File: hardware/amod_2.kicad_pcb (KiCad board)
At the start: 4 copper layers, 100 x 100 mm, 101 parts, among them J101 USB-C, J201 SMA, J202 SMA, J301 SMA, J302 SMA, J303 SMA, J304 SMA, J501 SMA, J502 SMA, J503 SMA, J504 SMA, J505 Pmod, Q301 AO3401A, Q501 AO3401A, SW301 ON, SW501 ON, U101 TPS65131, U102 LM2664, U201 THS3491, U301 OPA847, U501 LMH6629, U502 LMH6629

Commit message: AMOD-2 in progress: Y9 switched noise source, Y7 reflection bridge (INC and REFL = 2A - 2B), Y8 passive coupled resonators with capacitive ports
ERC 0, DRC 0.  IO8 reaches Y9 round the left and top margins; Y9's -5 V up a finger of L3 from the gutter.

Co-Authored-By: Claude Opus 5.5 <noreply@anthropic.com>
Claude-Session: https://claude.ai/code/session_01RKeoKvFFzjk3cEBLCXXHnB
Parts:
- added C701: 100n, Capacitor_SMD:C_0402_1005Metric, F.Cu at (23.4, 31.2)
- added C702: 100n, Capacitor_SMD:C_0402_1005Metric, F.Cu at (28.6, 31.2)
- added C703: 100n, Capacitor_SMD:C_0402_1005Metric, F.Cu at (16.9, 40.9)
- added C704: 100n, Capacitor_SMD:C_0402_1005Metric, F.Cu at (30.6, 42.8)
- added C801: 2.2p, Capacitor_SMD:C_0402_1005Metric, F.Cu at (18.1, 55.5)
- added C802: 4.7p, Capacitor_SMD:C_0402_1005Metric, F.Cu at (18.6, 53.5)
- added C803: 2.2p, Capacitor_SMD:C_0402_1005Metric, F.Cu at (23.0, 61.4)
- added C804: 1p, Capacitor_SMD:C_0402_1005Metric, F.Cu at (25.4, 57.1)
- added C805: 2.2p, Capacitor_SMD:C_0402_1005Metric, F.Cu at (26.6, 57.1)
- added C806: 1n, Capacitor_SMD:C_0402_1005Metric, F.Cu at (38.5, 53.4)
- added C807: 6.8p, Capacitor_SMD:C_0402_1005Metric, F.Cu at (45.8, 57.4)
- added C808: 2.2p, Capacitor_SMD:C_0402_1005Metric, F.Cu at (44.5, 61.4)
- added C809: 100n, Capacitor_SMD:C_0402_1005Metric, F.Cu at (16.8, 63.0)
- added C901: 1u, Capacitor_SMD:C_0402_1005Metric, F.Cu at (75.5, 8.35)
- added C902: 100n, Capacitor_SMD:C_0402_1005Metric, F.Cu at (78.6, 11.1)
- added C903: 100p, Capacitor_SMD:C_0402_1005Metric, F.Cu at (79.8, 18.1)
- added C904: 100n, Capacitor_SMD:C_0402_1005Metric, F.Cu at (78.7, 18.1)
- added C905: 1u, Capacitor_SMD:C_0402_1005Metric, F.Cu at (82.7, 12.5)
- added C906: 1u, Capacitor_SMD:C_0402_1005Metric, F.Cu at (83.3, 20.6)
- added C907: 1u, Capacitor_SMD:C_0402_1005Metric, F.Cu at (88.8, 13.3)
- added C908: 100n, Capacitor_SMD:C_0402_1005Metric, F.Cu at (81.2, 20.1)
- added D801: BB133, Diode_SMD:D_SOD-323, F.Cu at (24.9, 53.5)
- added D802: BB133, Diode_SMD:D_SOD-323, F.Cu at (26.9, 53.5)
- added D803: BB133, Diode_SMD:D_SOD-323, F.Cu at (42.6, 53.5)
- added D804: BB133, Diode_SMD:D_SOD-323, F.Cu at (44.8, 53.5)
- added J701: SMA, amod:SMA_BWSMA-KE-Z001_Vertical, F.Cu at (12.5, 34.0)
- added J702: SMA, amod:SMA_BWSMA-KE-Z001_Vertical, F.Cu at (23.0, 44.5)
- added J703: SMA, amod:SMA_BWSMA-KE-Z001_Vertical, F.Cu at (34.0, 34.0)
- added J704: SMA, amod:SMA_BWSMA-KE-Z001_Vertical, F.Cu at (44.5, 44.5)
- added J801: SMA, amod:SMA_BWSMA-KE-Z001_Vertical, F.Cu at (12.5, 55.5)
- added J802: SMA, amod:SMA_BWSMA-KE-Z001_Vertical, F.Cu at (23.0, 66.0)
- added J803: SMA, amod:SMA_BWSMA-KE-Z001_Vertical, F.Cu at (34.0, 55.5)
- added J804: SMA, amod:SMA_BWSMA-KE-Z001_Vertical, F.Cu at (44.5, 66.0)
- added J901: SMA, amod:SMA_BWSMA-KE-Z001_Vertical, F.Cu at (87.5, 23.0)
- added L801: 10u, Inductor_SMD:L_1210_3225Metric, F.Cu at (21.6, 52.6)
- added L802: 10u, Inductor_SMD:L_1210_3225Metric, F.Cu at (47.5, 53.4)
- added Q701: AO3401A, Package_TO_SOT_SMD:SOT-23, F.Cu at (15.3, 47.4)
- added Q801: AO3401A, Package_TO_SOT_SMD:SOT-23, F.Cu at (15.3, 68.8)
- added Q901: AO3401A, Package_TO_SOT_SMD:SOT-23, F.Cu at (79.8, 25.9)
- added Q902: MMBT3904, Package_TO_SOT_SMD:SOT-23, F.Cu at (78.8, 15.3)
- added R701: 49.9, Resistor_SMD:R_0402_1005Metric, F.Cu at (20.9, 34.0)
- added R702: 49.9, Resistor_SMD:R_0402_1005Metric, F.Cu at (19.9, 35.5)
- added R703: 49.9, Resistor_SMD:R_0402_1005Metric, F.Cu at (19.9, 37.5)
- added R704: 499, Resistor_SMD:R_0402_1005Metric, F.Cu at (22.6, 40.4)
- added R705: 499, Resistor_SMD:R_0402_1005Metric, F.Cu at (20.6, 40.4)
- added R706: 49.9, Resistor_SMD:R_0402_1005Metric, F.Cu at (24.6, 39.9)
- added R707: 499, Resistor_SMD:R_0402_1005Metric, F.Cu at (25.2, 37.6)
- added R708: 499, Resistor_SMD:R_0402_1005Metric, F.Cu at (27.6, 40.4)
- added R709: 49.9, Resistor_SMD:R_0402_1005Metric, F.Cu at (31.2, 39.2)
- added R801: 49.9, Resistor_SMD:R_0402_1005Metric, F.Cu at (16.6, 56.9)
- added R802: 100k, Resistor_SMD:R_0402_1005Metric, F.Cu at (28.8, 53.1)
- added R803: 100k, Resistor_SMD:R_0402_1005Metric, F.Cu at (28.8, 55.1)
- added R804: 2k, Resistor_SMD:R_0402_1005Metric, F.Cu at (27.8, 57.1)
- added R805: 100k, Resistor_SMD:R_0402_1005Metric, F.Cu at (39.6, 53.4)
- added R806: 100k, Resistor_SMD:R_0402_1005Metric, F.Cu at (40.9, 53.4)
- added R807: 2k, Resistor_SMD:R_0402_1005Metric, F.Cu at (39.0, 57.4)
- added R901: 680, Resistor_SMD:R_0402_1005Metric, F.Cu at (78.6, 12.7)
- added R902: 10k, Resistor_SMD:R_0402_1005Metric, F.Cu at (83.8, 11.1)
- added R903: 10k, Resistor_SMD:R_0402_1005Metric, F.Cu at (84.9, 11.1)
- added R904: 240, Resistor_SMD:R_0402_1005Metric, F.Cu at (85.8, 17.9)
- added R905: 27, Resistor_SMD:R_0402_1005Metric, F.Cu at (83.3, 18.6)
- added R906: 49.9, Resistor_SMD:R_0402_1005Metric, F.Cu at (88.8, 15.3)
- added SW701: ON, amod:SW_SPDT_Shouhan_MSK12C02, F.Cu at (10.5, 44.9)
- added SW801: ON, amod:SW_SPDT_Shouhan_MSK12C02, F.Cu at (10.5, 66.3)
- added SW802: DIP4, amod:SW_DIP_SPSTx04_Slide_1.27mm_DSHP04, F.Cu at (33.8, 65.0)
- added SW901: ON, amod:SW_SPDT_Shouhan_MSK12C02, F.Cu at (75.0, 23.4)
- added U701: OPA810, Package_TO_SOT_SMD:SOT-23-5, F.Cu at (22.4, 37.6)
- added U702: OPA810, Package_TO_SOT_SMD:SOT-23-5, F.Cu at (27.6, 37.6)
- added U901: TPS22917, Package_TO_SOT_SMD:SOT-23-6, F.Cu at (75.5, 10.8)
- added U902: LMH6629, Package_TO_SOT_SMD:SOT-23-5, F.Cu at (85.5, 14.7)
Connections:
- J505 pad 5: unconnected-(J505-Pin_5-Pad5) -> /PMOD8
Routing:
- net /PMOD8: track 0.00 -> 188.2 mm
- net /Y8_VS: track 0.00 -> 72.2 mm, vias 0 -> 4
- net /Y8_T2: track 0.00 -> 42.5 mm
- net /Y9_VS: track 0.00 -> 41.0 mm, vias 0 -> 4
- net GND: track 70.1 -> 105.8 mm, vias 57 -> 88
- net /Y7_VS: track 0.00 -> 27.7 mm, vias 0 -> 5
- net -5V: track 62.5 -> 87.7 mm, vias 6 -> 13
- net /Y8_T1: track 0.00 -> 23.3 mm
- net /Y7_REFL: track 0.00 -> 18.0 mm
- net /Y7_A: track 0.00 -> 15.2 mm
- net /Y9_OA: track 0.00 -> 11.0 mm
- net /Y8_RDA: track 0.00 -> 10.2 mm
- net /Y8_CB: track 0.00 -> 10.2 mm
- net /Y8_K2: track 0.00 -> 10.1 mm
- net /Y8_CA: track 0.00 -> 10.1 mm
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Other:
- board text added: "BRIDGE"
- board text added: "DRIVE"
- board text added: "DUT"
- board text added: "INC"
- board text added: "NOISE"
- board text added: "OUT 1"
- board text added: "OUT 2"
- board text added: "REFL"
- board text added: "REFL/INC=S11"
- board text added: "SIG"
- board text added: "TANKS"
- board text added: "TUNE/PUMP"
- board text added: "Y7"
- board text added: "Y8"
- board text added: "Y9"

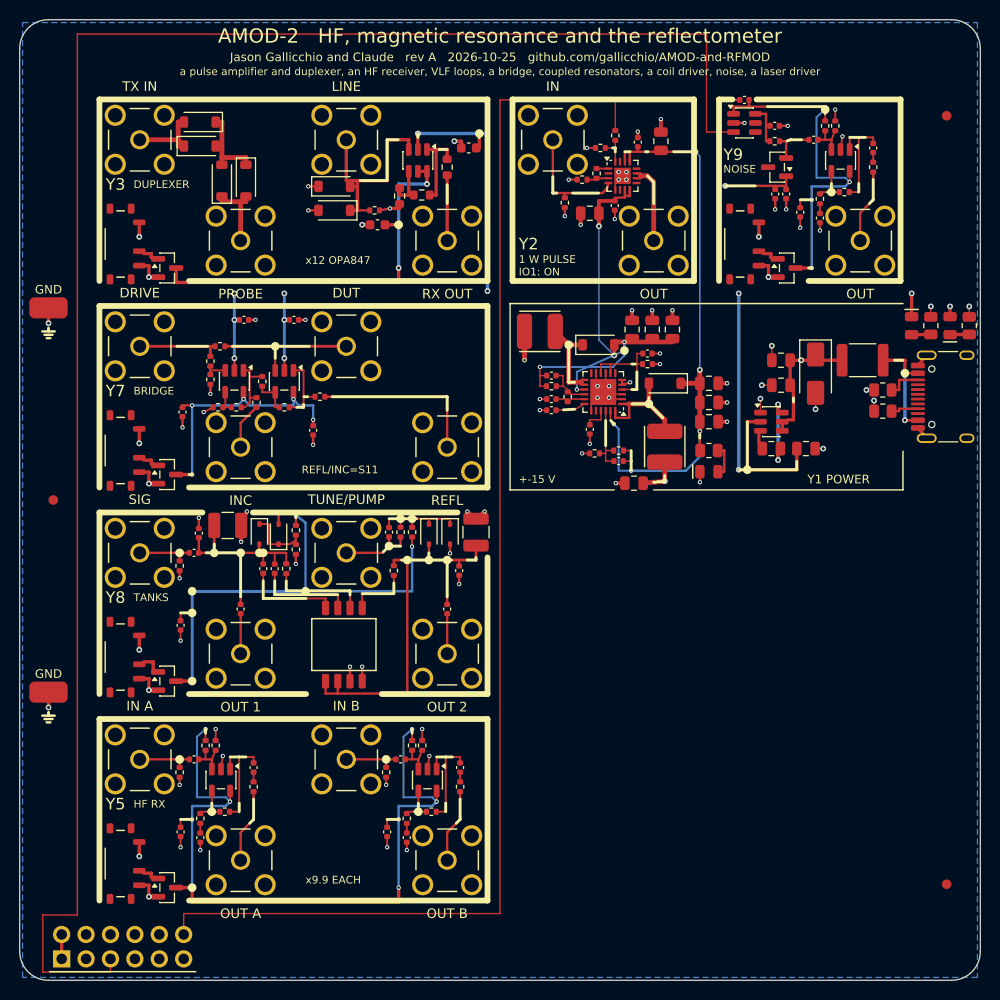
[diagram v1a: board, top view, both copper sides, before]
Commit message: AMOD-2 in progress: Y10 laser driver (100 mA/V high-side source, IO5 shunt, 20 MHz - 3 GHz bias-T, diode-voltage monitor)
ERC 0, DRC 0.  IO5 up the gutter at x 50.4; a foot moved off the LD jack.

Co-Authored-By: Claude Opus 5.5 <noreply@anthropic.com>
Claude-Session: https://claude.ai/code/session_01RKeoKvFFzjk3cEBLCXXHnB
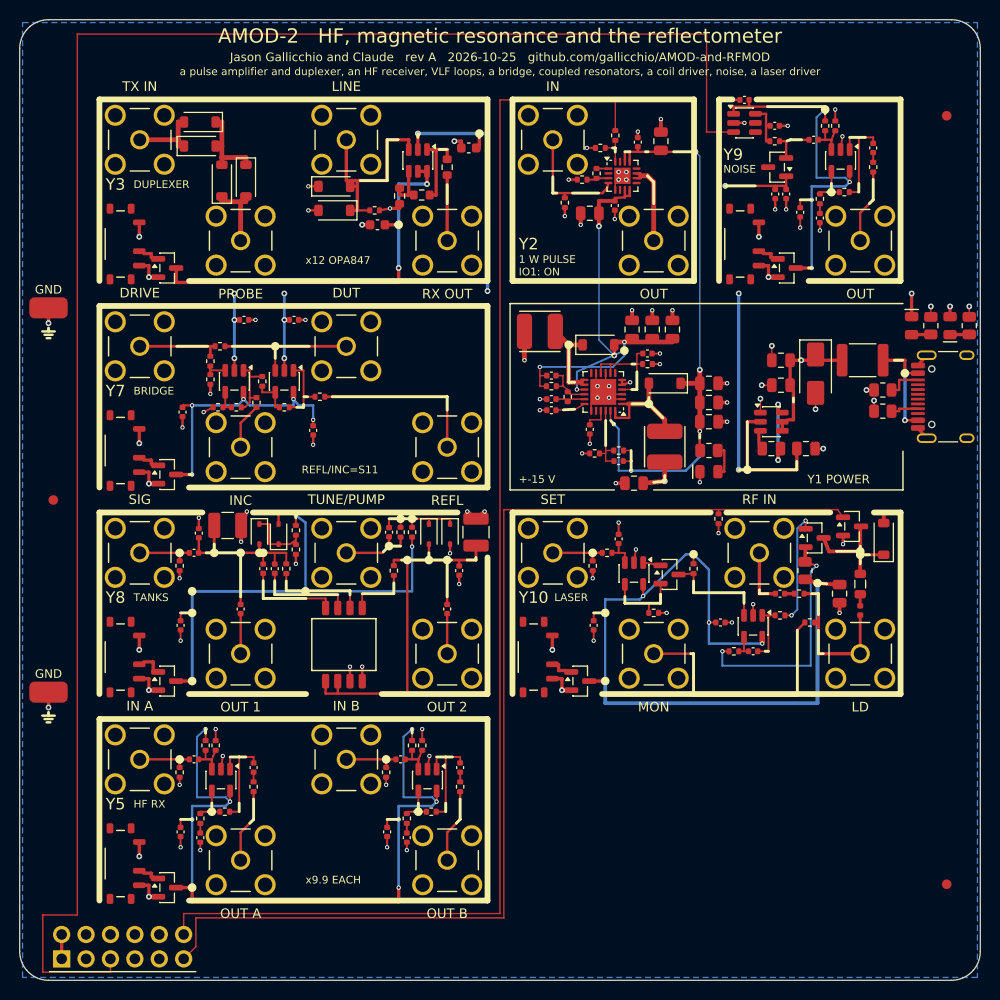
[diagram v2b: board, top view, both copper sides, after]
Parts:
- added C1001: 100n, Capacitor_SMD:C_0402_1005Metric, F.Cu at (62.4, 54.0)
- added C1002: 100n, Capacitor_SMD:C_0402_1005Metric, F.Cu at (59.8, 63.0)
- added C1003: 10n, Capacitor_SMD:C_0402_1005Metric, F.Cu at (76.3, 65.8)
- added C1004: 10u, Capacitor_SMD:C_0805_2012Metric, F.Cu at (85.3, 59.8)
- added C1005: 100p, Capacitor_SMD:C_0402_1005Metric, F.Cu at (79.2, 59.8)
- added C1006: 100n, Capacitor_SMD:C_0402_1005Metric, F.Cu at (73.0, 62.8)
- added D1001: B5819W, Diode_SMD:D_SOD-123, F.Cu at (90.0, 54.0)
- added J1001: SMA, amod:SMA_BWSMA-KE-Z001_Vertical, F.Cu at (55.5, 55.5)
- added J1002: SMA, amod:SMA_BWSMA-KE-Z001_Vertical, F.Cu at (66.0, 66.0)
- added J1003: SMA, amod:SMA_BWSMA-KE-Z001_Vertical, F.Cu at (77.0, 55.5)
- added J1004: SMA, amod:SMA_BWSMA-KE-Z001_Vertical, F.Cu at (87.5, 66.0)
- added L1001: 330n, Inductor_SMD:L_0805_2012Metric, F.Cu at (87.5, 58.8)
- added L1002: 27n, Inductor_SMD:L_0402_1005Metric, F.Cu at (87.5, 61.5)
- added Q1001: AO3401A, Package_TO_SOT_SMD:SOT-23, F.Cu at (58.4, 68.8)
- added Q1002: 2N7002, Package_TO_SOT_SMD:SOT-23, F.Cu at (67.7, 57.8)
- added Q1003: AO3401A, Package_TO_SOT_SMD:SOT-23, F.Cu at (82.8, 54.0)
- added Q1004: AO3400A, Package_TO_SOT_SMD:SOT-23, F.Cu at (86.7, 52.8)
- added R1001: 49.9, Resistor_SMD:R_0402_1005Metric, F.Cu at (59.6, 56.9)
- added R1002: 1k, Resistor_SMD:R_0402_1005Metric, F.Cu at (61.1, 55.5)
- added R1003: 1k, Resistor_SMD:R_0402_1005Metric, F.Cu at (66.0, 61.8)
- added R1004: 1k, Resistor_SMD:R_0402_1005Metric, F.Cu at (70.2, 57.1)
- added R1005: 100, Resistor_SMD:R_0402_1005Metric, F.Cu at (79.2, 62.0)
- added R1006: 1k, Resistor_SMD:R_0402_1005Metric, F.Cu at (74.3, 65.8)
- added R1007: 10, Resistor_SMD:R_0805_2012Metric, F.Cu at (81.8, 57.4)
- added R1008: 47, Resistor_SMD:R_0402_1005Metric, F.Cu at (81.2, 59.8)
- added R1009: 10k, Resistor_SMD:R_0402_1005Metric, F.Cu at (82.2, 62.8)
- added R1010: 100k, Resistor_SMD:R_0402_1005Metric, F.Cu at (72.8, 52.0)
- added SW1001: ON, amod:SW_SPDT_Shouhan_MSK12C02, F.Cu at (53.5, 66.3)
- added U1001: OPA810, Package_TO_SOT_SMD:SOT-23-5, F.Cu at (64.0, 57.6)
- added U1002: OPA810, Package_TO_SOT_SMD:SOT-23-5, F.Cu at (76.3, 63.1)
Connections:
- J505 pad 11: unconnected-(J505-Pin_11-Pad11) -> /PMOD5
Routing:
- net /PMOD5: track 0.00 -> 115.5 mm
- net /Y10_VS: track 0.00 -> 83.0 mm, vias 0 -> 7
- net /Y10_MON: track 0.00 -> 27.2 mm
- net /Y10_SQ: track 0.00 -> 24.9 mm, vias 0 -> 2
- net /Y10_LDN: track 0.00 -> 16.5 mm
- net GND: track 105.8 -> 118.6 mm, vias 88 -> 100
- net /Y10_ID: track 0.00 -> 12.2 mm
- net /Y10_GQ: track 0.00 -> 12.0 mm, vias 0 -> 2
- net /Y10_REF: track 0.00 -> 11.2 mm
- net /Y10_NS: track 0.00 -> 8.73 mm
- net /Y10_GA: track 0.00 -> 6.20 mm
- net /Y10_SET: track 0.00 -> 5.98 mm
- net /Y10_RF: track 0.00 -> 5.92 mm
- net /Y10_SETF: track 0.00 -> 3.32 mm
- net +5V: track 35.9 -> 39.0 mm, vias 10 -> 11
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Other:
- board text added: "LASER"
- board text added: "LD"
- board text added: "MON"
- board text added: "RF IN"
- board text added: "SET"
- board text added: "Y10"

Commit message: AMOD-2 rev A: all ten tiles (Y6 VLF loop amplifier, Y4 DRV8876 coil driver added); per-board fiducials
ERC 0, DRC 0.  IO6 / IO7 reach Y4 on the back along the bottom edge and across the top of Y6; the third fiducial
moves off Y4's coil terminal (FIDUCIALS in the board module, default unchanged).

Co-Authored-By: Claude Opus 5.5 <noreply@anthropic.com>
Claude-Session: https://claude.ai/code/session_01RKeoKvFFzjk3cEBLCXXHnB
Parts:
- added C401: 10u, Capacitor_SMD:C_0805_2012Metric, F.Cu at (88.8, 81.0)
- added C402: 22n, Capacitor_SMD:C_0402_1005Metric, F.Cu at (89.8, 84.1)
- added C403: 100n, Capacitor_SMD:C_0402_1005Metric, F.Cu at (90.8, 85.0)
- added C601: 1u, Capacitor_SMD:C_0402_1005Metric, F.Cu at (61.1, 77.0)
- added C602: 1u, Capacitor_SMD:C_0402_1005Metric, F.Cu at (61.8, 85.2)
- added C603: 100p, Capacitor_SMD:C_0402_1005Metric, F.Cu at (65.0, 83.5)
- added C604: 1u, Capacitor_SMD:C_0402_1005Metric, F.Cu at (67.3, 77.8)
- added C605: 100n, Capacitor_SMD:C_0402_1005Metric, F.Cu at (59.8, 84.5)
- added D401: B5819W, Diode_SMD:D_SOD-123, F.Cu at (88.2, 77.2)
- added D402: B5819W, Diode_SMD:D_SOD-123, F.Cu at (90.5, 76.5)
- added J401: SMA, amod:SMA_BWSMA-KE-Z001_Vertical, F.Cu at (77.0, 77.0)
- added J402: VM in, amod:TerminalBlock_KF301_1x02_P5.00mm, F.Cu at (95.7, 81.2)
- added J403: coil, amod:TerminalBlock_KF301_1x02_P5.00mm, F.Cu at (95.7, 93.2)
- added J601: SMA, amod:SMA_BWSMA-KE-Z001_Vertical, F.Cu at (55.5, 77.0)
- added J602: SMA, amod:SMA_BWSMA-KE-Z001_Vertical, F.Cu at (66.0, 87.5)
- added Q401: AO3401A, Package_TO_SOT_SMD:SOT-23, F.Cu at (79.8, 90.3)
- added Q601: AO3401A, Package_TO_SOT_SMD:SOT-23, F.Cu at (58.4, 90.3)
- added R401: 100k, Resistor_SMD:R_0402_1005Metric, F.Cu at (79.7, 82.0)
- added R402: 100k, Resistor_SMD:R_0402_1005Metric, F.Cu at (80.0, 83.2)
- added R403: 5.1k, Resistor_SMD:R_0402_1005Metric, F.Cu at (78.5, 84.2)
- added R404: 3.3k, Resistor_SMD:R_0402_1005Metric, F.Cu at (78.5, 86.2)
- added R405: 1.5k, Resistor_SMD:R_0402_1005Metric, F.Cu at (80.8, 87.3)
- added R406: 49.9, Resistor_SMD:R_0402_1005Metric, F.Cu at (82.2, 77.0)
- added R601: 100k, Resistor_SMD:R_0402_1005Metric, F.Cu at (62.4, 75.5)
- added R602: 100k, Resistor_SMD:R_0402_1005Metric, F.Cu at (63.4, 75.5)
- added R603: 10k, Resistor_SMD:R_0402_1005Metric, F.Cu at (64.3, 82.5)
- added R604: 100, Resistor_SMD:R_0402_1005Metric, F.Cu at (61.8, 83.2)
- added R605: 49.9, Resistor_SMD:R_0402_1005Metric, F.Cu at (67.3, 79.8)
- added SW401: ON, amod:SW_SPDT_Shouhan_MSK12C02, F.Cu at (75.0, 87.8)
- added SW601: ON, amod:SW_SPDT_Shouhan_MSK12C02, F.Cu at (53.5, 87.8)
- added U401: DRV8876, Package_SO:HTSSOP-16-1EP_4.4x5mm_P0.65mm_EP3.4x5mm_Mask2.66x2.46mm, F.Cu at (85.2, 84.8)
- added U402: OPA810, Package_TO_SOT_SMD:SOT-23-5, F.Cu at (84.8, 79.2)
- added U601: OPA810, Package_TO_SOT_SMD:SOT-23-5, F.Cu at (64.0, 79.2)
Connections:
- J505 pad 7: unconnected-(J505-Pin_7-Pad7) -> /PMOD7
- J505 pad 9: unconnected-(J505-Pin_9-Pad9) -> /PMOD6
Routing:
- net /PMOD7: track 0.00 -> 110.6 mm, vias 0 -> 1
- net /PMOD6: track 0.00 -> 108.1 mm, vias 0 -> 1
- net /Y4_VS: track 0.00 -> 44.1 mm, vias 0 -> 3
- net /Y6_VS: track 0.00 -> 29.8 mm, vias 0 -> 4
- net GND: track 118.6 -> 146.2 mm, vias 100 -> 117
- net /Y4_OUT1: track 0.00 -> 20.9 mm
- net /Y4_VM: track 0.00 -> 19.6 mm
- net /Y4_IP: track 0.00 -> 12.7 mm, vias 0 -> 2
- net /Y6_OA: track 0.00 -> 12.3 mm
- net /Y4_MO: track 0.00 -> 10.5 mm
- net /Y4_OUT2: track 0.00 -> 9.87 mm
- net /Y6_OUT: track 0.00 -> 7.70 mm
- net /Y4_VEXT: track 0.00 -> 7.58 mm
- net +5V: track 39.0 -> 45.3 mm, vias 11 -> 13
- net /Y6_FB: track 0.00 -> 5.69 mm
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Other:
- board text added: "COIL"
- board text added: "LOOP"
- board text added: "VLF"
- board text added: "Y4"
- board text added: "Y6"
